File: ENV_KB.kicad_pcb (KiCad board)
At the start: 2 copper layers, 348.1 x 156.3 mm, 200 parts, among them J0 TYPE-C-31-M-12

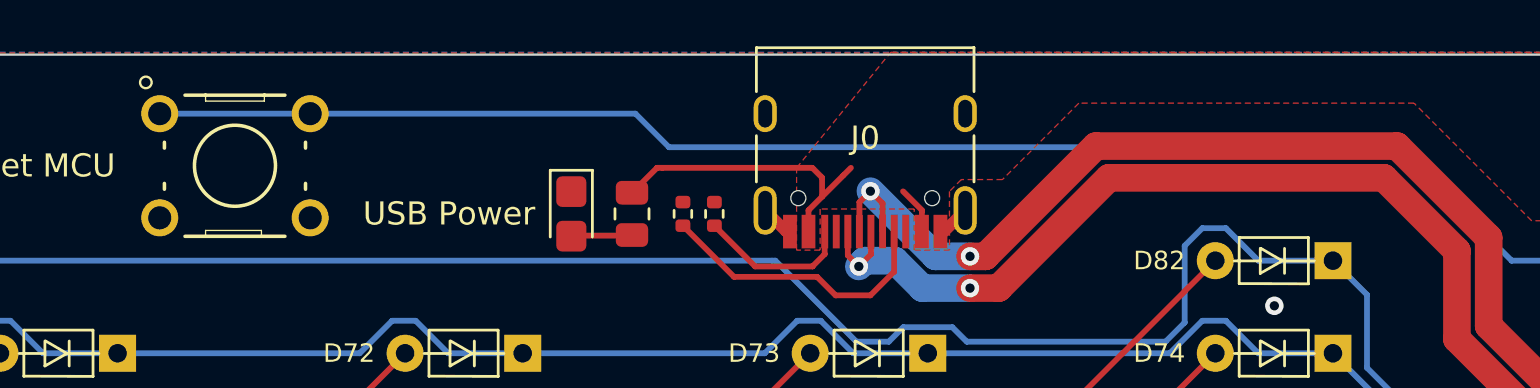
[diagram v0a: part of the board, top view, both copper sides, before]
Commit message: some plate adjustments and smaller reset button
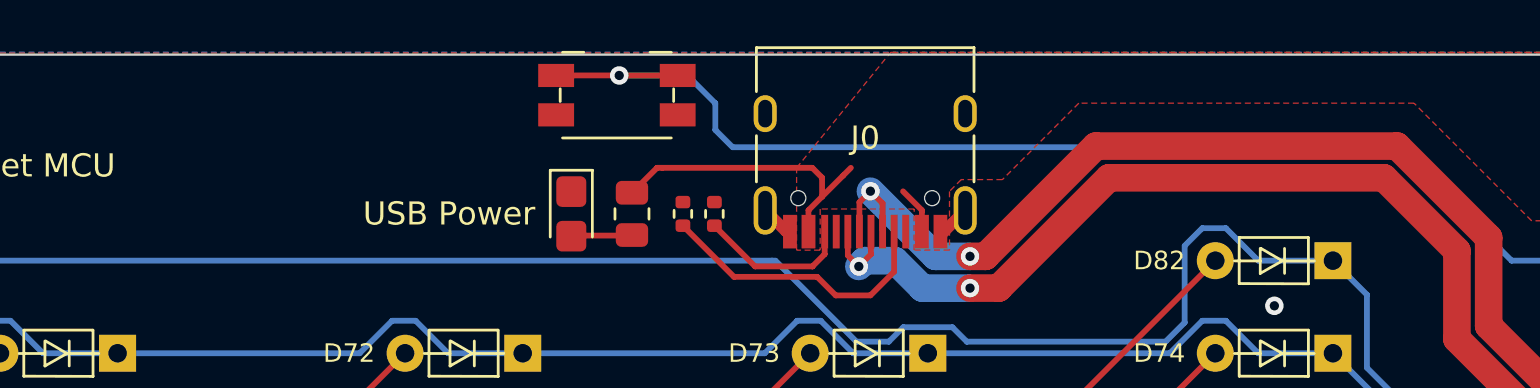
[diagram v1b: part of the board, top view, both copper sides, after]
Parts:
- SW-RST0: value B3F-1000 -> Reset Buton; footprint EM_Extras:SW_B3F-1000 -> Button_Switch_SMD:Panasonic_EVQPUJ_EVQPUA
- moved SW-RST0 16.8 mm to (297.8, 107.3)
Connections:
- SW-RST0 pad 2: Resetbtn -> GND
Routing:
- net Resetbtn: track 92.9 -> 79.7 mm, vias 1 -> 2

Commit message: Changed mount hole size and adjusted placement
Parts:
- H0, H1, H10, H2, H3, H4, H5, H6, H7, H8, H9: footprint MountingHole:MountingHole_2.2mm_M2 -> MountingHole:MountingHole_3.2mm_M3
- moved H0 4.46 mm to (143.6, 110.2)
- moved H1 4.19 mm to (474.0, 110.2)
- moved H10 0.97 mm to (474.1, 161.8)
- moved H9 0.30 mm to (144.2, 161.8)

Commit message: Redesigned Plate, resized board, adjusted mount holes
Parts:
- removed H2, H5, H8: MountingHole, MountingHole:MountingHole_3.2mm_M3
- moved H3 22.5 mm to (136.3, 258.2)
- moved H4 16.5 mm to (483.7, 258.3)
- moved H1 8.46 mm to (482.5, 110.4)
- moved H0 6.10 mm to (137.5, 110.4)
- moved H9 1.65 mm to (145.9, 161.8)
- moved J0 1.48 mm to (310.0, 109.0)
- moved PowerLED0 1.48 mm to (297.3, 112.3)
- moved PowerLedResistor0 1.48 mm to (299.9, 112.3)
- moved RESISTOR0 1.48 mm to (302.1, 112.3)
- moved RESISTOR1 1.48 mm to (303.5, 112.3)
- moved SW-RST0 1.48 mm to (299.3, 107.2)
- moved H6 1.45 mm to (310.0, 161.8)
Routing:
- net USB2_P: track 45.1 -> 47.9 mm, vias 3 -> 2
- net USB2_N: track 45.6 -> 48.4 mm, vias 3 -> 2
- net col9: track 181.0 -> 182.8 mm
- net Resetbtn: track 79.7 -> 78.6 mm
- net col0: track 353.1 -> 354.0 mm
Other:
- board size 348.1 x 156.3 mm -> 354.6 x 156.5 mm
- board text removed: "All mount holes are 2.2mm M2"
- board text removed: "Board Dimentions: 348.25mm*156.502mm"

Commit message: Updated Gerber bits and laser cut dxfs
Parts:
- moved H7 3.41 mm to (305.1, 257.1)
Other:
- outline, holes or cut-outs redrawn
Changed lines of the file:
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@@
   )
   (layers
-    (0 F.Cu signal)
-    (31 B.Cu signal)
-    (32 B.Adhes user)
-    (33 F.Adhes user)
-    (34 B.Paste user)
-    (35 F.Paste user)
-    (36 B.SilkS user)
-    (37 F.SilkS user)
-    (38 B.Mask user)
-    (39 F.Mask user)
-    (40 Dwgs.User user)
-    (41 Cmts.User user)
+    (0 F.Cu signal hide)
+    (31 B.Cu signal hide)
+    (32 B.Adhes user hide)
+    (33 F.Adhes user hide)
+    (34 B.Paste user hide)
+    (35 F.Paste user hide)
+    (36 B.SilkS user hide)
+    (37 F.SilkS user hide)
+    (38 B.Mask user hide)
+    (39 F.Mask user hide)
+    (40 Dwgs.User user hide)
+    (41 Cmts.User user hide)
     (42 Eco1.User user)
     (43 Eco2.User user)
     (44 Edge.Cuts user)
-    (45 Margin user)
-    (46 B.CrtYd user)
-    (47 F.CrtYd user)
-    (48 B.Fab user)
-    (49 F.Fab user)
+    (45 Margin user hide)
+    (46 B.CrtYd user hide)
+    (47 F.CrtYd user hide)
+    (48 B.Fab user hide)
+    (49 F.Fab user hide)
   )
   (setup
@@
     (visible_elements 7FFFFFFF)
     (pcbplotparams
-      (layerselection 0x010fc_ffffffff)
+      (layerselection 0x01800_7ffffffe)
       (usegerberextensions true)
       (usegerberattributes false)
       (usegerberadvancedattributes false)
       (creategerberjobfile false)
-      (excludeedgelayer true)
+      (excludeedgelayer false)
       (linewidth 0.150000)
       (plotframeref false)
@@
       (padsonsilk false)
       (subtractmaskfromsilk true)
-      (outputformat 1)
+      (outputformat 3)
       (mirror false)
       (drillshape 0)
@@
   )
   (module MountingHole:MountingHole_3.2mm_M3 (layer F.Cu)
-    (at 308.55 257.15)
+    (at 305.1375 257.15)
     (descr "Mounting Hole 3.2mm, no annular, M3")
     (tags "mounting hole 3.2mm no annular m3")
@@
       (effects (font (size 0.25 0.25) (thickness 0.0625)))
     )
-    (fp_text user %R (at 0.04 0.7 90) (layer F.Fab)
-      (effects (font (size 0.26 0.26) (thickness 0.04)))
-    )
     (fp_line (start -0.525 0.27) (end -0.525 -0.27) (layer F.Fab) (width 0.1))
     (fp_line (start -0.525 -0.27) (end 0.525 -0.27) (layer F.Fab) (width 0.1))
@@
     (fp_line (start 0.93 -0.47) (end 0.93 0.47) (layer F.CrtYd) (width 0.05))
     (fp_line (start 0.93 0.47) (end -0.93 0.47) (layer F.CrtYd) (width 0.05))
+    (fp_text user %R (at 0.04 0.7 90) (layer F.Fab)
+      (effects (font (size 0.26 0.26) (thickness 0.04)))
+    )
     (pad 1 smd roundrect (at -0.51 0 270) (size 0.54 0.64) (layers F.Cu F.Paste F.Mask) (roundrect_rratio 0.25)
       (net 116 GND))
@@
       (effects (font (size 0.25 0.25) (thickness 0.05)))
     )
-    (fp_text user %R (at -1.83 0.25 180) (layer F.Fab)
-      (effects (font (size 0.1 0.1) (thickness 0.025)))
-    )
     (fp_line (start -1 0.625) (end -1 -0.625) (layer F.Fab) (width 0.1))
     (fp_line (start -1 -0.625) (end 1 -0.625) (layer F.Fab) (width 0.1))
@@
     (fp_line (start 1.68 -0.95) (end 1.68 0.95) (layer F.CrtYd) (width 0.05))
     (fp_line (start 1.68 0.95) (end -1.68 0.95) (layer F.CrtYd) (width 0.05))
+    (fp_text user %R (at -1.83 0.25 180) (layer F.Fab)
+      (effects (font (size 0.1 0.1) (thickness 0.025)))
+    )
     (pad 1 smd roundrect (at -0.9125 0 270) (size 1.025 1.4) (layers F.Cu F.Paste F.Mask) (roundrect_rratio 0.2439004878048781)
       (net 113 USBVBUS))
@@
       (effects (font (size 1 1) (thickness 0.015)))
     )
-    (fp_text user %R (at 0 -0.005 180) (layer F.Fab)
-      (effects (font (size 1 1) (thickness 0.15)))
-    )
     (fp_line (start -4.7 3.9) (end 4.7 3.9) (layer F.SilkS) (width 0.12))
     (fp_line (start -4.47 -3.65) (end 4.47 -3.65) (layer F.Fab) (width 0.1))
@@
     (fp_line (start -4.7 -1.9) (end -4.7 0.1) (layer F.SilkS) (width 0.12))
     (fp_line (start -4.7 2) (end -4.7 3.9) (layer F.SilkS) (width 0.12))
+    (fp_text user %R (at 0 -0.005 180) (layer F.Fab)
+      (effects (font (size 1 1) (thickness 0.15)))
+    )
     (pad S1 thru_hole oval (at 4.32 1.05 180) (size 1 1.6) (drill oval 0.6 1.2) (layers *.Cu *.Mask)
       (net 116 GND))
@@
       (xy 11.939978 0.656972) (xy 12.153863 0.64183) (xy 12.295317 0.661551)) (layer F.Mask) (width 0.01))
   )
-  (gr_circle (center 136.321564 258.25) (end 137.646564 257.325) (layer Eco1.User) (width 0.1))
-  (gr_circle (center 308.546564 257.15) (end 309.871564 256.225) (layer Eco1.User) (width 0.1))
-  (gr_circle (center 483.721564 258.3) (end 485.046564 257.375) (layer Eco1.User) (width 0.1))
-  (gr_circle (center 474.096564 161.8) (end 475.421564 160.875) (layer Eco1.User) (width 0.1))
-  (gr_circle (center 310.021564 161.825) (end 311.346564 160.9) (layer Eco1.User) (width 0.1))
-  (gr_circle (center 145.896564 161.8) (end 147.221564 160.875) (layer Eco1.User) (width 0.1))
-  (gr_circle (center 137.496564 110.4) (end 138.821564 109.475) (layer Eco1.User) (width 0.1))
-  (gr_circle (center 482.497379 110.4) (end 483.797379 109.4) (layer Eco1.User) (width 0.1))
+  (gr_circle (center 136.321564 258.25) (end 137.646564 257.325) (layer Edge.Cuts) (width 0.1))
+  (gr_circle (center 305.1375 257.15) (end 306.4625 256.225) (layer Edge.Cuts) (width 0.1))
+  (gr_circle (center 483.721564 258.3) (end 485.046564 257.375) (layer Edge.Cuts) (width 0.1))
+  (gr_circle (center 474.096564 161.8) (end 475.421564 160.875) (layer Edge.Cuts) (width 0.1))
+  (gr_circle (center 310.021564 161.825) (end 311.346564 160.9) (layer Edge.Cuts) (width 0.1))
+  (gr_circle (center 145.896564 161.8) (end 147.221564 160.875) (layer Edge.Cuts) (width 0.1))
+  (gr_circle (center 137.496564 110.4) (end 138.821564 109.475) (layer Edge.Cuts) (width 0.1))
+  (gr_circle (center 482.497379 110.4) (end 483.797379 109.4) (layer Edge.Cuts) (width 0.1))
   (gr_line (start 407.7745 221.701) (end 407.7745 222.7) (layer Eco2.User) (width 0.1))
   (gr_arc (start 415.34625 212.17094) (end 415.34625 211.67094) (angle -90) (layer Eco2.User) (width 0.1))

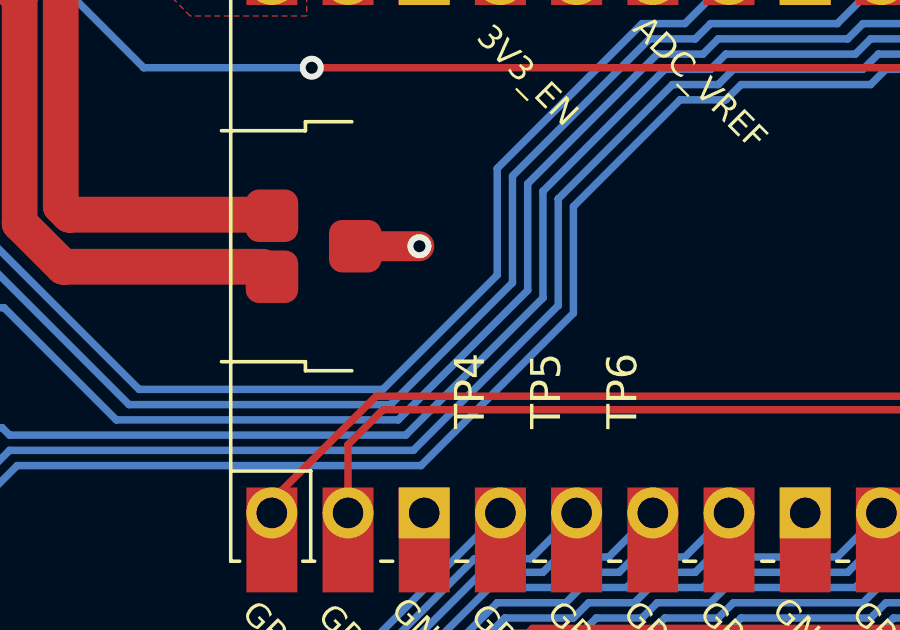
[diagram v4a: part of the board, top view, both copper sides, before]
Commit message: a few small adjustments to traces and pads
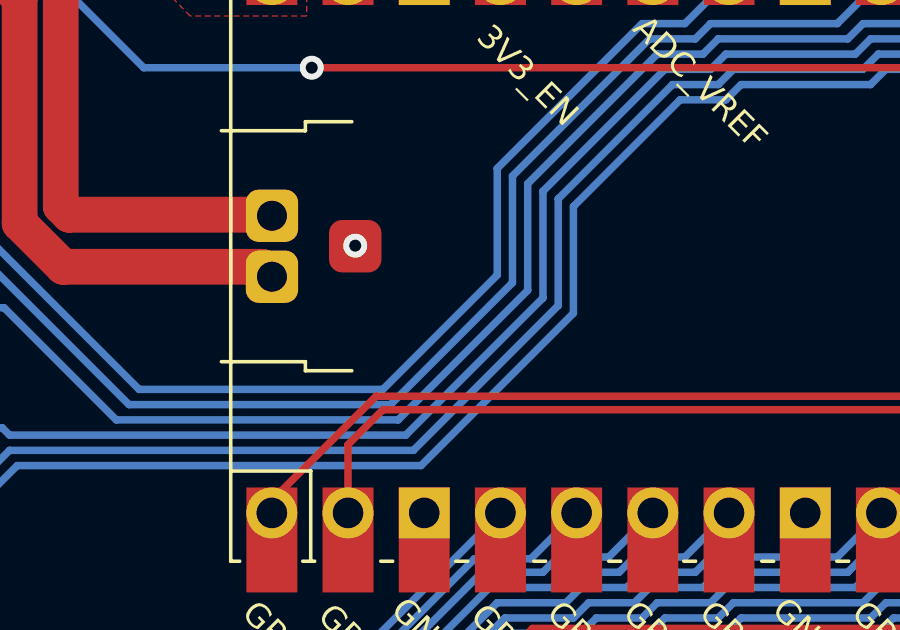
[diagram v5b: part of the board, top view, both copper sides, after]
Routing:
- net GND: track 7.52 -> 5.38 mm

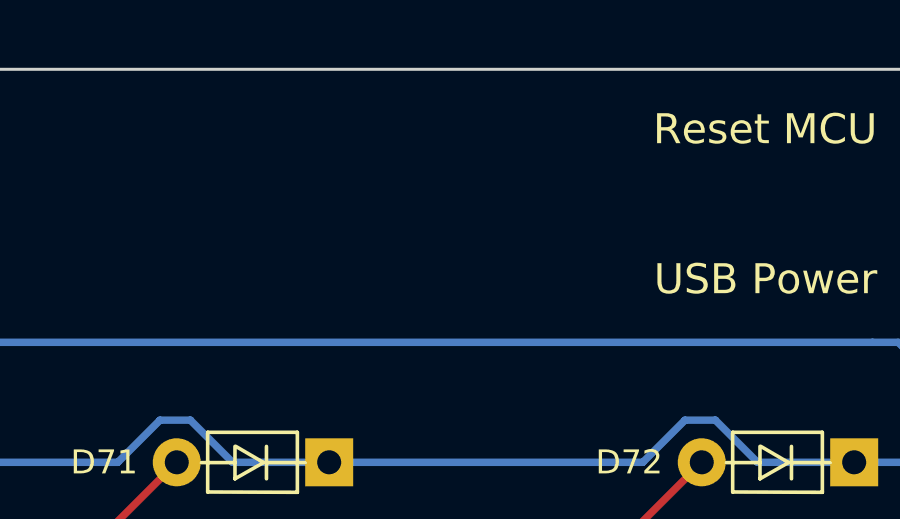
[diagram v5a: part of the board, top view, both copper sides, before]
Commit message: Added a new mount hole and updated gerber files
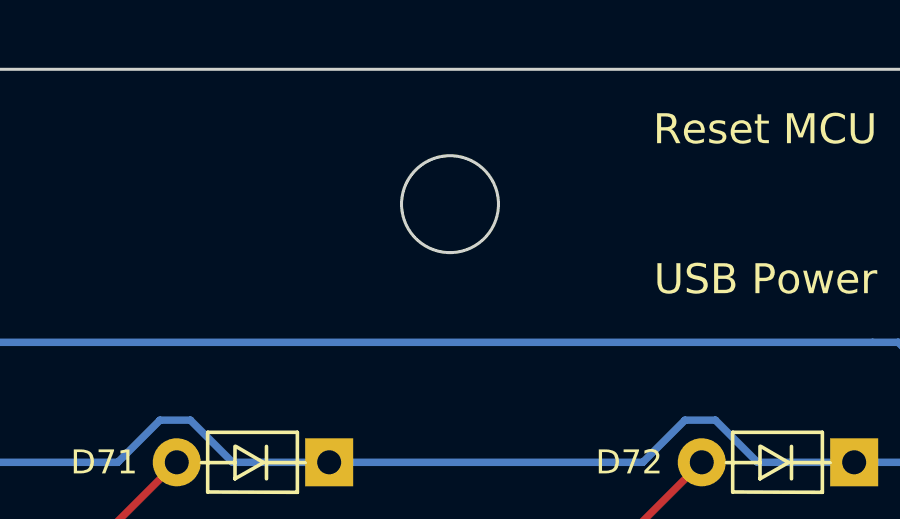
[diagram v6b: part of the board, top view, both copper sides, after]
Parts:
- added H8: MountingHole, MountingHole:MountingHole_3.2mm_M3, F.Cu at (280.3, 109.9)
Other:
- outline, holes or cut-outs redrawn
